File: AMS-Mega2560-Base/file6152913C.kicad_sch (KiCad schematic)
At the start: 43 parts, among them IC14 LTV-814, IC15 LTV-814, IC16 LTV-814, IC17 DS3231SN#, IC18 MAX232CPE+, Q10 2N7000, Q11 PSMP033-60YEX, Q12 PSMP033-60YEX, Q13 PSMP033-60YEX, Q5 2N7000, Q6 2N7000, Q7 2N7000, Q8 2N7000, Q9 2N7000, U3 S8411-45R

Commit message: fixing some library settings and updating some schematics
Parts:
- IC14, IC15, IC16: footprint DIP762W60P254L460H450Q4N -> SamacSys_Parts:DIP762W60P254L460H450Q4N
- Q11, Q12, Q13: footprint PSMP03360YEX -> SamacSys_Parts:PSMP03360YEX
- R30, R31, R32, R33, R34, R35, R36, R37, R38, R39, R40, R41, R42, R43, R44, R45, R46, R47, R48, R49: footprint Resistor_THT:R_Axial_DIN0207_L6.3mm_D2.5mm_P5.08mm_Vertical -> Resistor_THT:R_Axial_DIN0207_L6.3mm_D2.5mm_P2.54mm_Vertical
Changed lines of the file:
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@@
       (effects (font (size 1.27 1.27)) (justify left))
     )
-    (property "Footprint" "Resistor_THT:R_Axial_DIN0207_L6.3mm_D2.5mm_P5.08mm_Vertical" (id 2) (at 229.362 149.86 90)
+    (property "Footprint" "Resistor_THT:R_Axial_DIN0207_L6.3mm_D2.5mm_P2.54mm_Vertical" (id 2) (at 229.362 149.86 90)
       (effects (font (size 1.27 1.27)) hide)
     )
@@
       (effects (font (size 1.27 1.27)) (justify left))
     )
-    (property "Footprint" "Resistor_THT:R_Axial_DIN0207_L6.3mm_D2.5mm_P5.08mm_Vertical" (id 2) (at 234.442 97.79 90)
+    (property "Footprint" "Resistor_THT:R_Axial_DIN0207_L6.3mm_D2.5mm_P2.54mm_Vertical" (id 2) (at 234.442 97.79 90)
       (effects (font (size 1.27 1.27)) hide)
     )
@@
       (effects (font (size 1.27 1.27)) (justify left))
     )
-    (property "Footprint" "Resistor_THT:R_Axial_DIN0207_L6.3mm_D2.5mm_P5.08mm_Vertical" (id 2) (at 36.322 104.14 90)
+    (property "Footprint" "Resistor_THT:R_Axial_DIN0207_L6.3mm_D2.5mm_P2.54mm_Vertical" (id 2) (at 36.322 104.14 90)
       (effects (font (size 1.27 1.27)) hide)
     )
@@
       (effects (font (size 1.27 1.27)) (justify left))
     )
-    (property "Footprint" "Resistor_THT:R_Axial_DIN0207_L6.3mm_D2.5mm_P5.08mm_Vertical" (id 2) (at 225.552 52.07 90)
+    (property "Footprint" "Resistor_THT:R_Axial_DIN0207_L6.3mm_D2.5mm_P2.54mm_Vertical" (id 2) (at 225.552 52.07 90)
       (effects (font (size 1.27 1.27)) hide)
     )
@@
       (effects (font (size 1.27 1.27)) (justify left))
     )
-    (property "Footprint" "Resistor_THT:R_Axial_DIN0207_L6.3mm_D2.5mm_P5.08mm_Vertical" (id 2) (at 74.422 31.75 90)
+    (property "Footprint" "Resistor_THT:R_Axial_DIN0207_L6.3mm_D2.5mm_P2.54mm_Vertical" (id 2) (at 74.422 31.75 90)
       (effects (font (size 1.27 1.27)) hide)
     )
@@
       (effects (font (size 1.27 1.27)) (justify left))
     )
-    (property "Footprint" "Resistor_THT:R_Axial_DIN0207_L6.3mm_D2.5mm_P5.08mm_Vertical" (id 2) (at 36.322 62.23 90)
+    (property "Footprint" "Resistor_THT:R_Axial_DIN0207_L6.3mm_D2.5mm_P2.54mm_Vertical" (id 2) (at 36.322 62.23 90)
       (effects (font (size 1.27 1.27)) hide)
     )
@@
       (effects (font (size 1.27 1.27)) (justify left))
     )
-    (property "Footprint" "Resistor_THT:R_Axial_DIN0207_L6.3mm_D2.5mm_P5.08mm_Vertical" (id 2) (at 36.322 142.24 90)
+    (property "Footprint" "Resistor_THT:R_Axial_DIN0207_L6.3mm_D2.5mm_P2.54mm_Vertical" (id 2) (at 36.322 142.24 90)
       (effects (font (size 1.27 1.27)) hide)
     )
@@
       (effects (font (size 1.27 1.27)) (justify left))
     )
-    (property "Footprint" "Resistor_THT:R_Axial_DIN0207_L6.3mm_D2.5mm_P5.08mm_Vertical" (id 2) (at 184.912 95.25 90)
+    (property "Footprint" "Resistor_THT:R_Axial_DIN0207_L6.3mm_D2.5mm_P2.54mm_Vertical" (id 2) (at 184.912 95.25 90)
       (effects (font (size 1.27 1.27)) hide)
     )
@@
       (effects (font (size 1.27 1.27)) (justify left))
     )
-    (property "Footprint" "Resistor_THT:R_Axial_DIN0207_L6.3mm_D2.5mm_P5.08mm_Vertical" (id 2) (at 191.262 95.25 90)
+    (property "Footprint" "Resistor_THT:R_Axial_DIN0207_L6.3mm_D2.5mm_P2.54mm_Vertical" (id 2) (at 191.262 95.25 90)
       (effects (font (size 1.27 1.27)) hide)
     )
@@
     (property "Reference" "Q11" (id 0) (at 255.27 33.401 0))
     (property "Value" "PSMP033-60YEX" (id 1) (at 255.27 31.0896 0))
-    (property "Footprint" "PSMP03360YEX" (id 2) (at 246.38 29.21 0)
+    (property "Footprint" "SamacSys_Parts:PSMP03360YEX" (id 2) (at 246.38 29.21 0)
       (effects (font (size 1.27 1.27)) (justify left) hide)
     )
@@
       (effects (font (size 1.27 1.27)) (justify left))
     )
-    (property "Footprint" "Resistor_THT:R_Axial_DIN0207_L6.3mm_D2.5mm_P5.08mm_Vertical" (id 2) (at 233.172 31.75 90)
+    (property "Footprint" "Resistor_THT:R_Axial_DIN0207_L6.3mm_D2.5mm_P2.54mm_Vertical" (id 2) (at 233.172 31.75 90)
       (effects (font (size 1.27 1.27)) hide)
     )
@@
       (effects (font (size 1.27 1.27)) (justify left))
     )
-    (property "Footprint" "Resistor_THT:R_Axial_DIN0207_L6.3mm_D2.5mm_P5.08mm_Vertical" (id 2) (at 233.172 21.59 90)
+    (property "Footprint" "Resistor_THT:R_Axial_DIN0207_L6.3mm_D2.5mm_P2.54mm_Vertical" (id 2) (at 233.172 21.59 90)
       (effects (font (size 1.27 1.27)) hide)
     )
@@
     (property "Reference" "Q13" (id 0) (at 264.16 80.391 0))
     (property "Value" "PSMP033-60YEX" (id 1) (at 264.16 78.0796 0))
-    (property "Footprint" "PSMP03360YEX" (id 2) (at 255.27 76.2 0)
+    (property "Footprint" "SamacSys_Parts:PSMP03360YEX" (id 2) (at 255.27 76.2 0)
       (effects (font (size 1.27 1.27)) (justify left) hide)
     )
@@
       (effects (font (size 1.27 1.27)) (justify left))
     )
-    (property "Footprint" "Resistor_THT:R_Axial_DIN0207_L6.3mm_D2.5mm_P5.08mm_Vertical" (id 2) (at 242.062 78.74 90)
+    (property "Footprint" "Resistor_THT:R_Axial_DIN0207_L6.3mm_D2.5mm_P2.54mm_Vertical" (id 2) (at 242.062 78.74 90)
       (effects (font (size 1.27 1.27)) hide)
     )
@@
       (effects (font (size 1.27 1.27)) (justify left))
     )
-    (property "Footprint" "Resistor_THT:R_Axial_DIN0207_L6.3mm_D2.5mm_P5.08mm_Vertical" (id 2) (at 242.062 68.58 90)
+    (property "Footprint" "Resistor_THT:R_Axial_DIN0207_L6.3mm_D2.5mm_P2.54mm_Vertical" (id 2) (at 242.062 68.58 90)
       (effects (font (size 1.27 1.27)) hide)
     )
@@
     (property "Reference" "Q12" (id 0) (at 259.08 132.461 0))
     (property "Value" "PSMP033-60YEX" (id 1) (at 259.08 130.1496 0))
-    (property "Footprint" "PSMP03360YEX" (id 2) (at 250.19 128.27 0)
+    (property "Footprint" "SamacSys_Parts:PSMP03360YEX" (id 2) (at 250.19 128.27 0)
       (effects (font (size 1.27 1.27)) (justify left) hide)
     )
@@
       (effects (font (size 1.27 1.27)) (justify left))
     )
-    (property "Footprint" "Resistor_THT:R_Axial_DIN0207_L6.3mm_D2.5mm_P5.08mm_Vertical" (id 2) (at 236.982 130.81 90)
+    (property "Footprint" "Resistor_THT:R_Axial_DIN0207_L6.3mm_D2.5mm_P2.54mm_Vertical" (id 2) (at 236.982 130.81 90)
       (effects (font (size 1.27 1.27)) hide)
     )
@@
       (effects (font (size 1.27 1.27)) (justify left))
     )
-    (property "Footprint" "Resistor_THT:R_Axial_DIN0207_L6.3mm_D2.5mm_P5.08mm_Vertical" (id 2) (at 236.982 120.65 90)
+    (property "Footprint" "Resistor_THT:R_Axial_DIN0207_L6.3mm_D2.5mm_P2.54mm_Vertical" (id 2) (at 236.982 120.65 90)
       (effects (font (size 1.27 1.27)) hide)
     )
@@
       (effects (font (size 1.27 1.27)) (justify left))
     )
-    (property "Footprint" "Resistor_THT:R_Axial_DIN0207_L6.3mm_D2.5mm_P5.08mm_Vertical" (id 2) (at 74.422 111.76 90)
+    (property "Footprint" "Resistor_THT:R_Axial_DIN0207_L6.3mm_D2.5mm_P2.54mm_Vertical" (id 2) (at 74.422 111.76 90)
       (effects (font (size 1.27 1.27)) hide)
     )
@@
       (effects (font (size 1.27 1.27)) (justify left))
     )
-    (property "Footprint" "Resistor_THT:R_Axial_DIN0207_L6.3mm_D2.5mm_P5.08mm_Vertical" (id 2) (at 99.822 111.76 90)
+    (property "Footprint" "Resistor_THT:R_Axial_DIN0207_L6.3mm_D2.5mm_P2.54mm_Vertical" (id 2) (at 99.822 111.76 90)
       (effects (font (size 1.27 1.27)) hide)
     )
@@
       (effects (font (size 1.27 1.27)) (justify left))
     )
-    (property "Footprint" "Resistor_THT:R_Axial_DIN0207_L6.3mm_D2.5mm_P5.08mm_Vertical" (id 2) (at 99.822 31.75 90)
+    (property "Footprint" "Resistor_THT:R_Axial_DIN0207_L6.3mm_D2.5mm_P2.54mm_Vertical" (id 2) (at 99.822 31.75 90)
       (effects (font (size 1.27 1.27)) hide)
     )
@@
       (effects (font (size 1.27 1.27)) (justify left))
     )
-    (property "Footprint" "Resistor_THT:R_Axial_DIN0207_L6.3mm_D2.5mm_P5.08mm_Vertical" (id 2) (at 74.422 73.66 90)
+    (property "Footprint" "Resistor_THT:R_Axial_DIN0207_L6.3mm_D2.5mm_P2.54mm_Vertical" (id 2) (at 74.422 73.66 90)
       (effects (font (size 1.27 1.27)) hide)
     )
@@
     (property "Reference" "IC14" (id 0) (at 88.9 34.1843 0))
     (property "Value" "LTV-814" (id 1) (at 88.9 36.9594 0))
-    (property "Footprint" "DIP762W60P254L460H450Q4N" (id 2) (at 96.52 38.1 0)
+    (property "Footprint" "SamacSys_Parts:DIP762W60P254L460H450Q4N" (id 2) (at 96.52 38.1 0)
       (effects (font (size 1.27 1.27)) (justify left) hide)
     )
@@
     (property "Reference" "IC15" (id 0) (at 88.9 76.0943 0))
     (property "Value" "LTV-814" (id 1) (at 88.9 78.8694 0))
-    (property "Footprint" "DIP762W60P254L460H450Q4N" (id 2) (at 96.52 80.01 0)
+    (property "Footprint" "SamacSys_Parts:DIP762W60P254L460H450Q4N" (id 2) (at 96.52 80.01 0)
       (effects (font (size 1.27 1.27)) (justify left) hide)
     )
@@
       (effects (font (size 1.27 1.27)) (justify left))
     )
-    (property "Footprint" "Resistor_THT:R_Axial_DIN0207_L6.3mm_D2.5mm_P5.08mm_Vertical" (id 2) (at 99.822 73.66 90)
+    (property "Footprint" "Resistor_THT:R_Axial_DIN0207_L6.3mm_D2.5mm_P2.54mm_Vertical" (id 2) (at 99.822 73.66 90)
       (effects (font (size 1.27 1.27)) hide)
     )
@@
     (property "Reference" "IC16" (id 0) (at 88.9 114.1943 0))
     (property "Value" "LTV-814" (id 1) (at 88.9 116.9694 0))
-    (property "Footprint" "DIP762W60P254L460H450Q4N" (id 2) (at 96.52 118.11 0)
-      (effects (font (size 1.27 1.27)) (justify left) hide)
-    )
+    (property "Footprint" "SamacSys_Parts:DIP762W60P254L460H450Q4N" (id 2) (at 96.52 118.11 0)
+      (effects (font (size 1.27 1.27)) (justify left) hide)
+    )

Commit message: BaseBoard fixes and updates. doing schematic work.
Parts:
- removed D5, D6, D7: 1N4007, Diode_THT:D_DO-41_SOD81_P10.16mm_Horizontal, symbol Diode:1N4007
- removed IC14, IC15, IC16: LTV-814, SamacSys_Parts:DIP762W60P254L460H450Q4N, symbol Samac_Sys:LTV-814
- removed Q10, Q5, Q6, Q7, Q8, Q9: 2N7000, Package_TO_SOT_THT:TO-92_Inline, symbol Transistor_FET:2N7000
- removed Q11, Q12, Q13: PSMP033-60YEX, SamacSys_Parts:PSMP03360YEX, symbol SamacSys_Parts:PSMP033-60YEX
- removed R30, R31, R32, R33, R34, R35, R36, R37, R38, R41, R42, R43, R44, R45, R46, R47, R48, R49: R, Resistor_THT:R_Axial_DIN0207_L6.3mm_D2.5mm_P2.54mm_Vertical, symbol Device:R
- renumbered IC17 to IC16, IC18 to IC17, R39 to R37, R40 to R38
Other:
- moved on the sheet: C36, C37, C38, C39, C40, IC16, IC17, R37, R38, U3

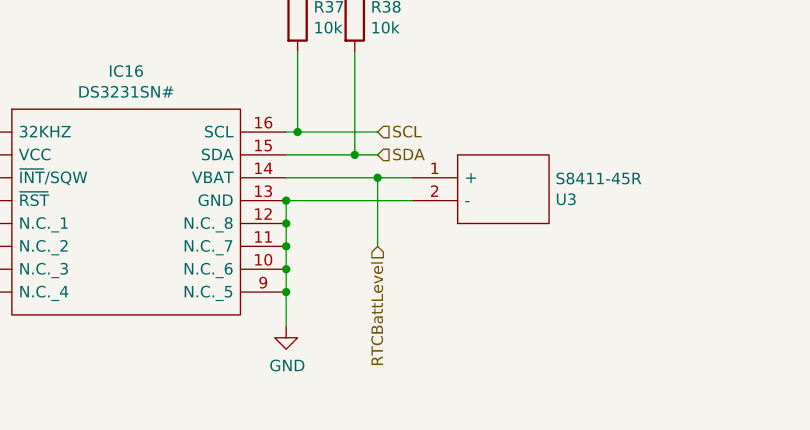
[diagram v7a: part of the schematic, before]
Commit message: I think everything is placed on the board special routes have been done. need to finish routing everything else.
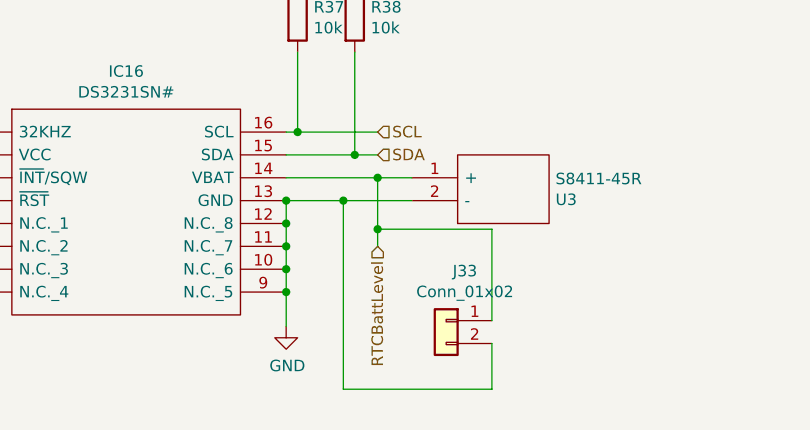
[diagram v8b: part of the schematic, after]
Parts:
- added J33: Conn_01x02, Connector_PinHeader_2.54mm:PinHeader_1x02_P2.54mm_Vertical, symbol Connector_Generic:Conn_01x02
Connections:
- net GND: now also J33.2 (Pin_2)
- net RTCBattLevel: now also J33.1 (Pin_1)
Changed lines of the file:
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@@
 (kicad_sch (version 20211123) (generator eeschema)
   (paper "A4")
+  (junction (at 78.74 51.435) (diameter 0) (color 0 0 0 0)
+  )
   (junction (at 68.58 50.8) (diameter 0) (color 0 0 0 0)
   )
@@
   )
   (junction (at 76.2 43.18) (diameter 0) (color 0 0 0 0)
+  )
+  (junction (at 74.93 48.26) (diameter 0) (color 0 0 0 0)
   )
   (junction (at 33.02 58.42) (diameter 0) (color 0 0 0 0)
@@
     (stroke (width 0) (type default) (color 0 0 0 0))
   )
+  (wire (pts (xy 91.44 69.215) (xy 74.93 69.215))
+    (stroke (width 0) (type default) (color 0 0 0 0))
+  )
   (wire (pts (xy 69.85 40.64) (xy 68.58 40.64))
     (stroke (width 0) (type default) (color 0 0 0 0))
@@
     (stroke (width 0) (type default) (color 0 0 0 0))
   )
+  (wire (pts (xy 91.44 51.435) (xy 78.74 51.435))
+    (stroke (width 0) (type default) (color 0 0 0 0))
+  )
   (wire (pts (xy 68.58 62.23) (xy 68.58 58.42))
     (stroke (width 0) (type default) (color 0 0 0 0))
@@
     (stroke (width 0) (type default) (color 0 0 0 0))
   )
+  (wire (pts (xy 74.93 69.215) (xy 74.93 48.26))
+    (stroke (width 0) (type default) (color 0 0 0 0))
+  )
   (wire (pts (xy 152.4 50.8) (xy 152.4 43.18))
     (stroke (width 0) (type default) (color 0 0 0 0))
@@
     (stroke (width 0) (type default) (color 0 0 0 0))
   )
+  (wire (pts (xy 78.74 51.435) (xy 78.74 45.72))
+    (stroke (width 0) (type default) (color 0 0 0 0))
+  )
   (wire (pts (xy 76.2 31.75) (xy 76.2 43.18))
     (stroke (width 0) (type default) (color 0 0 0 0))
   )
-  (wire (pts (xy 68.58 48.26) (xy 82.55 48.26))
-    (stroke (width 0) (type default) (color 0 0 0 0))
-  )
-  (wire (pts (xy 78.74 53.34) (xy 78.74 45.72))
+  (wire (pts (xy 68.58 48.26) (xy 74.93 48.26))
+    (stroke (width 0) (type default) (color 0 0 0 0))
+  )
+  (wire (pts (xy 78.74 53.34) (xy 78.74 51.435))
+    (stroke (width 0) (type default) (color 0 0 0 0))
+  )
+  (wire (pts (xy 91.44 64.135) (xy 91.44 69.215))
     (stroke (width 0) (type default) (color 0 0 0 0))
   )
@@
     (stroke (width 0) (type default) (color 0 0 0 0))
   )
+  (wire (pts (xy 74.93 48.26) (xy 82.55 48.26))
+    (stroke (width 0) (type default) (color 0 0 0 0))
+  )
   (wire (pts (xy 190.5 43.18) (xy 195.58 43.18))
     (stroke (width 0) (type default) (color 0 0 0 0))
@@
   )
   (wire (pts (xy 76.2 43.18) (xy 68.58 43.18))
+    (stroke (width 0) (type default) (color 0 0 0 0))
+  )
+  (wire (pts (xy 91.44 61.595) (xy 91.44 51.435))
     (stroke (width 0) (type default) (color 0 0 0 0))
   )
@@
     (pin "9")
   )
+  (symbol (lib_id "Connector_Generic:Conn_01x02") (at 86.36 61.595 0) (mirror y) (unit 1)
+    (in_bom yes) (on_board yes)
+    (property "Reference" "J33" (id 0) (at 88.4428 56.0832 0))
+    (property "Value" "Conn_01x02" (id 1) (at 88.4428 58.3946 0))
+    (property "Footprint" "Connector_PinHeader_2.54mm:PinHeader_1x02_P2.54mm_Vertical" (id 2) (at 86.36 61.595 0)
+      (effects (font (size 1.27 1.27)) hide)
+    )
+    (property "Datasheet" "~" (id 3) (at 86.36 61.595 0)
+      (effects (font (size 1.27 1.27)) hide)
+    )
+    (pin "1")
+    (pin "2")
+  )
 )
